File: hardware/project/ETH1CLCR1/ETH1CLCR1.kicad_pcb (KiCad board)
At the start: 6 copper layers, 160 x 100 mm, 705 parts, among them J1201 C64AC, J1301 Conn_02x05, J301 Conn_02x01, J302 Conn_02x05, J601 Conn_02x05, K1201 HE3621A0510, K1202 HE3621A0510, K1203 HE3621A0510, K1204 HE3621A0510, K1205 HE3621A0510, K1206 HE3621A0510, K701 9012, K702 9012, K703 9012, K704 9012, K801 TQ2SA-5V, M101 60817-096, Q1101 BC847, Q1102 BC847, Q1103 BC847, Q1104 BC847, Q501 IRFR5410, Q701 BC847, Q702 BC847, Q703 BC847, Q704 BC847, Q705 MMBT4401L, Q706 MMBT4403L, Q801 BC847W, Q802 2N2218A, Q803 2N2904A, Q804 BC847W, Q805 BC847W, Q806 BC847W, Q807 BC847W, Q808 BC847W, Q901 BC847W, Q902 BC847W, Q903 BC847W, U1001 TL074, U1002 TL074, U1003 REF192, U1004 DAC8568IBPWR, U1101 ADG419BR, U1102 ADG419BR, U1103 REF192, U1104 AD8606-2-MSOP, U1105 AD8606-2-MSOP, U1106 AD7380, U1107 AD8605, U1108 LT6350, U1109 LT6350, U1110 OPA602, U1111 OPA602, U1112 PGA103, U1113 PGA103, U1201 ULN2003A, U1301 24LC08B-E/MS, U1302 STM32H743ZI, U1401 ECS-3225SMV-500-GP-TR, U1402 REF192, U1403 74AHCT1G08, U1404 AD5689BRUZ, U1405 AD9835, U1406 TL072, U1407 DG419LDY, U1408 AD5453YRMZ, U1409 LT1468, U1410 LT1468, U1411 LT1468, U1501 LT8330_S6, U1502 LT8330_S6, U1503 MC7815BD2TG, U1504 MC7915BD2TG, U1505 MC78M12ABDTRKG, U1506 MC79M12CDTG, U1507 TSR2-2450, U1508 TSR1-2490, U1509 LM1117IMP-3.3/NOPB, U1510 LM1117IMP-3.3/NOPB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

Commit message: Checked the schematics. Created BOM.
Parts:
- removed the C1433 at (331.2, 11.4)
- removed the C1434 at (313.6, 17.0)
- added C1410: 100n, Capacitor_SMD:C_0603_1608Metric_Pad1.05x0.95mm_HandSolder, F.Cu at (166.9, 148.3)
- added C1417: 10n, Capacitor_SMD:C_0603_1608Metric_Pad1.05x0.95mm_HandSolder, F.Cu at (171.6, 145.4)
- added C1435: 10u, Capacitor_SMD:C_0805_2012Metric_Pad1.15x1.40mm_HandSolder, F.Cu at (167.1, 145.6)
- added C607: 1u, Capacitor_SMD:C_0603_1608Metric_Pad1.05x0.95mm_HandSolder, F.Cu at (37.2, 119.5)
- added R1422: DNP, Resistor_SMD:R_0603_1608Metric_Pad1.05x0.95mm_HandSolder, F.Cu at (173.1, 149.4)
- C1434: renamed from C1431; value C -> 1p5
- C1436: renamed from C1435; value C -> 1p5
- D705, D706: value 1N4149 -> 1N4148
- D707, D708: value SML4757A -> CMDZ5256B TR; footprint Diode_SMD:D_SMA -> Diode_SMD:D_SOD-323_HandSoldering
- J1301, J302, J601: value Conn_02x05 -> 20021111-00010T4LF
- Q1101, Q1102, Q1103, Q1104, Q701, Q702, Q703, Q704: value BC847 -> BC847W; footprint Package_TO_SOT_SMD:SOT-23 -> Package_TO_SOT_SMD:SOT-323_SC-70
- R1403, R1404, R912, R915, R918: value NC -> DNP
- R1420, R1421: value R -> 0
- R1428: renamed from R1427; value R -> DNP
- R824: value RN732BTTD9002B25 -> 90k
- R825, R830: value RN732ATTE1002B25 -> 10k
- R826: value RP73PF2A10RBTDF -> 10
- R827: value RT1206BRB07100RL -> 100
- R828: value TNPW08051K01BEEA -> 1k01
- R829: value RN73R2BTTD1001B25 -> 1k
- R906, R908, R909, R910, R911, R913, R917, R919: value RQ73C2A3K01BTDF -> 3k01
- R921, R923: value PAT1206E9000BST1 -> 900
- R922, R924: value RN73R2BTTD1000B25 -> 100
- U1509, U1510: value LM1117IMP-3.3/NOPB -> LM1117DTX-3.3/NOPB
- U1511: value LM1117IMP-5.0/NOPB -> LM1117DTX-5.0/NOPB
- U503: value LM1117IMP-3.3/NOPB -> LM1117DTX-3.3/NOPB; footprint Package_TO_SOT_SMD:SOT-223-3_TabPin2 -> Package_TO_SOT_SMD:TO-252-2
- moved Q702 203.2 mm to (256.5, 79.8)
- moved Q701 203.2 mm to (256.5, 76.2)
- moved Q703 203.2 mm to (261.0, 76.2)
- moved Q704 198.8 mm to (261.0, 79.8)
- moved Q1102 85.7 mm to (21.3, 123.7), turned to 0 degrees
- moved Q1103 82.3 mm to (25.7, 120.1), turned to 0 degrees
- moved Q1101 81.3 mm to (21.3, 120.1), turned to 0 degrees
- moved Q1104 76.3 mm to (25.7, 123.7), turned to 0 degrees
- moved U503 1.97 mm to (203.6, 119.8)
- renumbered C1403 to C1402, C1402 to C1403, C1406 to C1405, C1405 to C1406, C1410 to C1412, C1414 to C1413, C1412 to C1414, C1413 to C1416, C1416 to C1418, C1417 to C1419, C1418 to C1420, C1419 to C1421, C1420 to C1422, C1422 to C1423, C1421 to C1424, C1423 to C1425, C1425 to C1426, C1424 to C1427, C1426 to C1428, C1427 to C1429, C1429 to C1430, C1428 to C1431, C1430 to C1432, C1432 to C1433, C607 to C608, C608 to C609, C609 to C610, C610 to C611, C611 to C612, R1409 to R1407, R1407 to R1408, R1408 to R1409, R1413 to R1411, R1411 to R1412, R1412 to R1413, R1422 to R1423, R1423 to R1424, R1424 to R1425, R1425 to R1426, R1426 to R1427
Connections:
- net /FGEN Buffer + Source resistor/SR100CTR renamed /FGEN Buffer + Source resistor/SR_100CTR
- net /FGEN Buffer + Source resistor/SR10CTR renamed /FGEN Buffer + Source resistor/SR_10CTR
- net /FGEN Buffer + Source resistor/SR10KCTR renamed /FGEN Buffer + Source resistor/SR_10KCTR
- net /FGEN Buffer + Source resistor/SR1KCTR renamed /FGEN Buffer + Source resistor/SR_1KCTR
- net /MCU2/HA3-COMP renamed /MCU2/RR_HA3-COMP
- net /MCU2/R100CRT renamed /MCU2/RR_100CRT
- net /MCU2/R100KCRT renamed /MCU2/RR_100KCRT
- net /MCU2/R10CRT renamed /MCU2/RR_10CRT
- net /MCU2/R10KCRT renamed /MCU2/RR_10KCRT
- net /MCU2/R1KCRT renamed /MCU2/RR_1KCRT
- net /MCU2/RELAY_CTR renamed /MCU2/RR_RELAYCTR
- U1405 pad 3: (no net) -> Net-(C1417-Pad1)

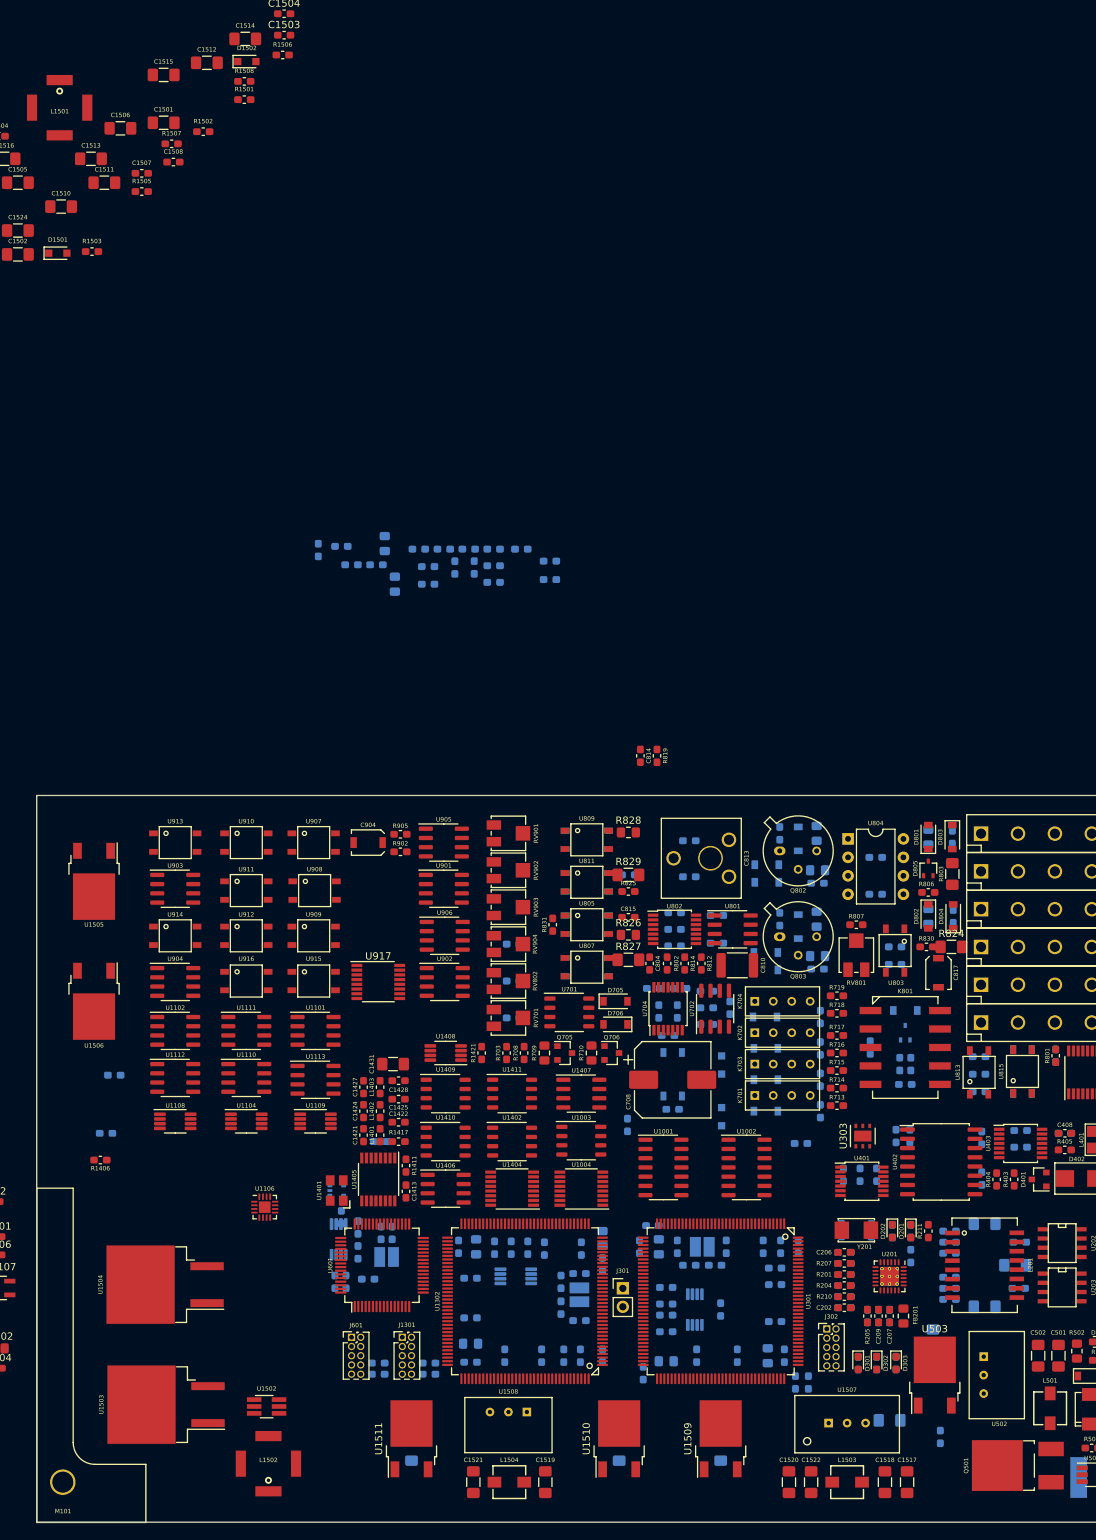
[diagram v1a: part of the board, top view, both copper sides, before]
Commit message: Fixed some mistakes in the foorpeints. BOM list ready.
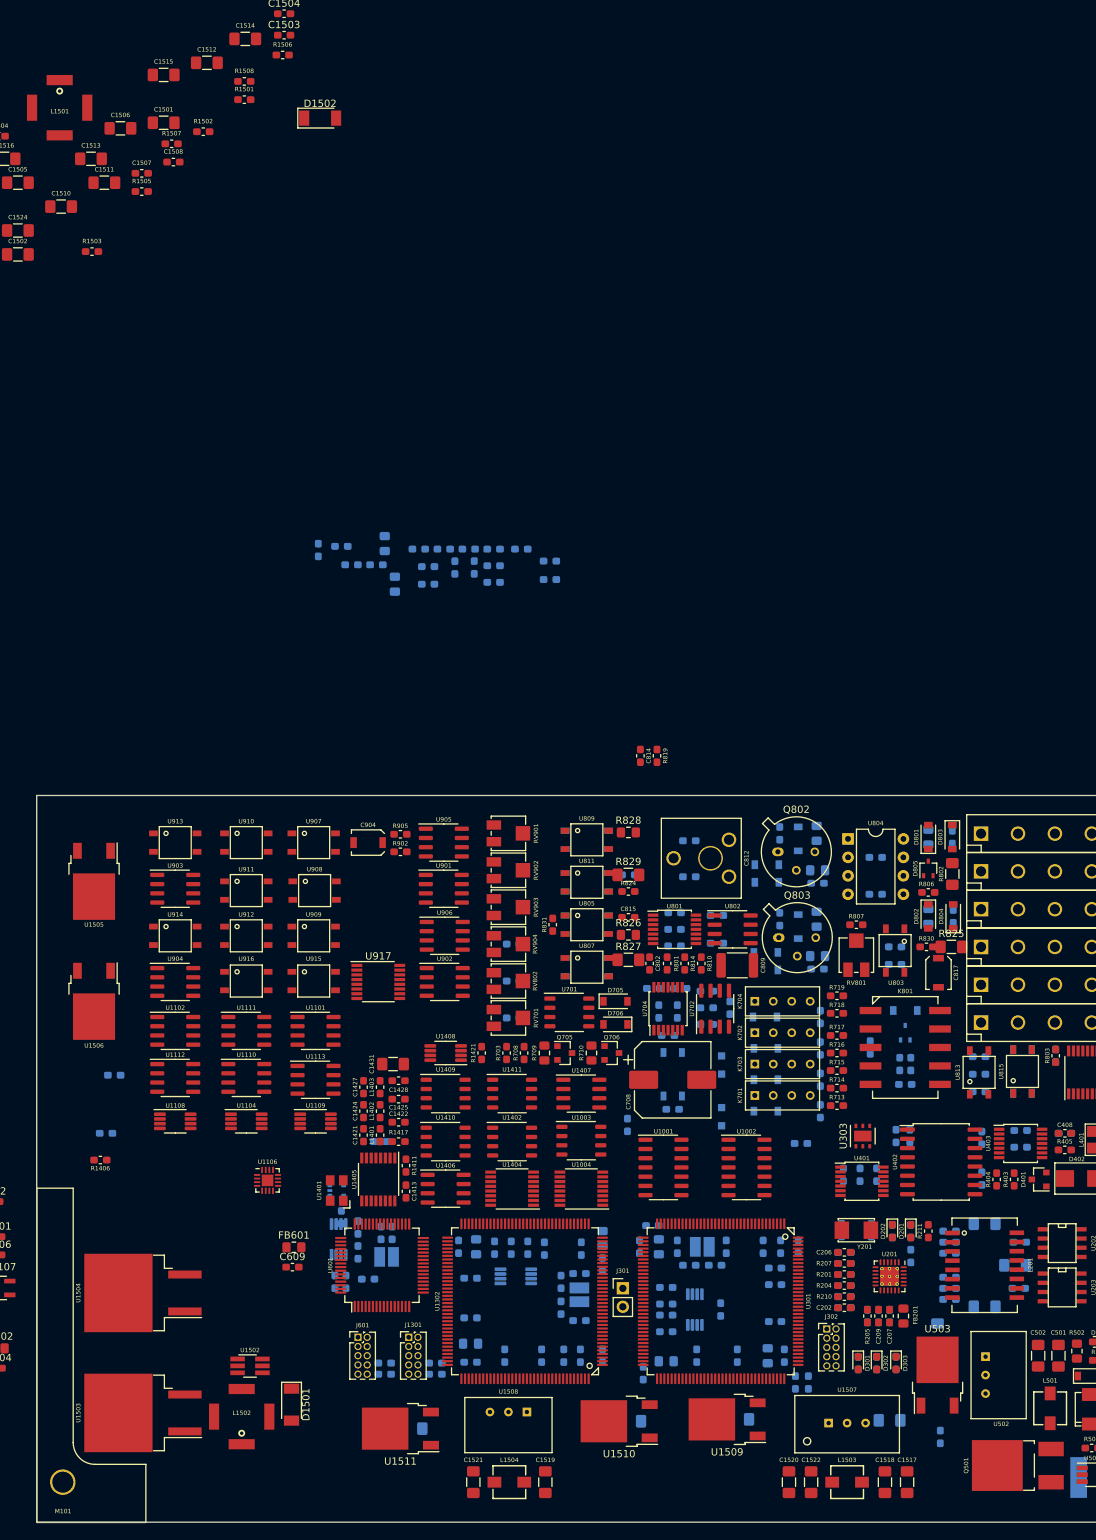
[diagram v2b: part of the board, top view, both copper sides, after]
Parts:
- added C609: 1u, Capacitor_SMD:C_0603_1608Metric_Pad1.05x0.95mm_HandSolder, F.Cu at (115.2, 104.9)
- added FB601: 742792031, Inductor_SMD:L_0805_2012Metric_Pad1.15x1.40mm_HandSolder, F.Cu at (115.4, 102.2)
- C708: value EEHZC1V221V -> 220u
- C713: value 43p/300V -> 43p/200V
- C809: renamed from C810; value 1u/150V -> 1u/100V
- C814: value 33p/300V -> 33p/200V
- D1501, D1502: value PMEG6010CEJ -> PMEG6010EP,115; footprint Diode_SMD:D_SOD-323_HandSoldering -> Diode_SMD:D_SOD-128
- R801: renamed from R802; value 1k -> 2k2
- moved D1501 161.7 mm to (115.1, 123.8), turned to 270 degrees
- moved D1502 12.7 mm to (119.0, -53.2)
- moved L1502 7.45 mm to (108.2, 125.5)
- moved U1502 6.04 mm to (109.3, 118.5)
- moved C1525 4.84 mm to (176.5, 125.9), turned to 0 degrees
- moved C1526 4.22 mm to (161.7, 126.1), turned to 0 degrees
- moved U1106 3.70 mm to (111.8, 93.0)
- moved U1503 3.37 mm to (94.6, 125.0)
- moved U1504 3.26 mm to (94.6, 108.5)
- moved C1527 2.92 mm to (131.6, 127.1), turned to 0 degrees
- moved U1509 2.81 mm to (175.0, 125.9), turned to 180 degrees
- moved U1510 2.41 mm to (160.1, 126.1), turned to 180 degrees
- moved U1511 2.07 mm to (130.0, 127.1), turned to 180 degrees
- moved C504 1.05 mm to (204.0, 114.1)
- moved J1301 0.89 mm to (131.2, 114.6)
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- renumbered C609 to C610, C610 to C611, C611 to C612, C612 to C613, C804 to C802, C805 to C803, C806 to C804, C802 to C805, C803 to C806, C809 to C810, C812 to C811, C813 to C812, C811 to C813, R803 to R802, R801 to R803, R809 to R808, R808 to R809, R812 to R810, R810 to R811, R811 to R812, R825 to R824, R824 to R825, U802 to U801, U801 to U802
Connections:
- net /MCU2/PA_NULL renamed /MCU2/PA_ER
- net /Process Amplifier/NULL_NPN renamed /Process Amplifier/ER_NPN
- Q802 pad 1: Net-(D806-Pad2) -> Net-(D810-Pad2)
- Q802 pad 2: Net-(D810-Pad2) -> Net-(D806-Pad2)
- Q803 pad 1: Net-(D807-Pad1) -> Net-(D811-Pad1)
- Q803 pad 2: Net-(D811-Pad1) -> Net-(D807-Pad1)
- R946 pad 1: /ADC/Eref -> Net-(R946-Pad1)
- U601 pad 13: +3.3VF -> /MCU3/VDDA
- U916 pad 3: AGNDF -> Net-(R946-Pad1)
- U916 pad 4: /ADC/Em -> /ADC/Eref

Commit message: PCB layout
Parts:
- removed M101: 60817-096, ETH1CLCR1:60817-096
- added C1506: 10u/50V, Capacitor_SMD:C_1206_3216Metric_Pad1.42x1.75mm_HandSolder, F.Cu at (97.4, 123.3)
- added C1507: 10u/50V, Capacitor_SMD:C_1206_3216Metric_Pad1.42x1.75mm_HandSolder, F.Cu at (114.8, 133.5)
- added C715: 10u/35V, Capacitor_SMD:C_1206_3216Metric_Pad1.42x1.75mm_HandSolder, F.Cu at (54.2, 36.4)
- added C716: 10u/35V, Capacitor_SMD:C_1206_3216Metric_Pad1.42x1.75mm_HandSolder, F.Cu at (54.2, 39.7)
- added C823: 10u/35V, Capacitor_SMD:C_1206_3216Metric_Pad1.42x1.75mm_HandSolder, B.Cu at (195.5, 45.2)
- added C824: 10u/35V, Capacitor_SMD:C_1206_3216Metric_Pad1.42x1.75mm_HandSolder, B.Cu at (195.5, 50.8)
- C1514: renamed from C1505; moved to B.Cu
- C1515: renamed from C1506; moved to B.Cu
- C1516: renamed from C1507; moved to B.Cu
- C1519: renamed from C1509; moved to B.Cu
- C1520: renamed from C1510; moved to B.Cu
- C1522: renamed from C1511; moved to B.Cu
- C1523: renamed from C1512; moved to B.Cu
- C1524: renamed from C1513; moved to B.Cu
- C1525: renamed from C1514; moved to B.Cu
- C1526: renamed from C1524; moved to B.Cu
- C322, C609, C705, C706, C814, D1501, D1502, FB601, Q701, Q702, Q703, Q704, R1506, R1507, R1508, R819, R825, R902, R905, U908, U910, U912: moved to B.Cu
- C816: moved to F.Cu
- moved Q801 227.6 mm to (219.7, 79.6), turned to 270 degrees
- moved R1506 197.5 mm to (84.2, 133.3), turned to 90 degrees
- moved R1501 189.5 mm to (95.8, 133.3), turned to 270 degrees
- moved R1504 186.5 mm to (104.5, 133.3)
- moved R1502 184.8 mm to (98.2, 133.3), turned to 90 degrees
- moved U1504 184.4 mm to (91.1, 133.3)
- moved C1525 182.6 mm to (112.4, 118.5), turned to 180 degrees
- moved C1510 181.1 mm to (97.4, 128.5), turned to 270 degrees
- moved L1502 180.7 mm to (90.6, 125.9), turned to 270 degrees
- moved C1516 179.1 mm to (86.5, 133.3), turned to 270 degrees
- moved C1515 179.0 mm to (112.1, 126.0), turned to 180 degrees
- moved R1508 177.7 mm to (104.6, 119.4)
- moved R1505 176.6 mm to (86.5, 133.3), turned to 270 degrees
- moved D1502 175.8 mm to (88.5, 119.9), turned to 270 degrees
- moved C1523 175.6 mm to (107.6, 114.7), turned to 270 degrees
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- renumbered C1517 to C1501, C1518 to C1502, C1520 to C1503, C1522 to C1504, C1523 to C1505, C1525 to C1508, C1526 to C1509, C1501 to C1510, C1502 to C1511, C1503 to C1512, C1504 to C1513, C1508 to C1517, C1519 to C1518, C1515 to C1527, C1516 to C1528, C1527 to C1529, L1503 to L1501, L1501 to L1502, L1502 to L1503, U1507 to U1501, U1509 to U1502, U1510 to U1503, U1501 to U1504, U1502 to U1505, U1503 to U1506, U1504 to U1507, U1511 to U1509, U1505 to U1510, U1506 to U1511

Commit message: PCB layout
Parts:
- added C1437: 100n, Capacitor_SMD:C_0603_1608Metric_Pad1.05x0.95mm_HandSolder, B.Cu at (135.3, 75.2)
- added C1438: 100n, Capacitor_SMD:C_0603_1608Metric_Pad1.05x0.95mm_HandSolder, B.Cu at (145.4, 89.8)
- added C911: 100n, Capacitor_SMD:C_0603_1608Metric_Pad1.05x0.95mm_HandSolder, B.Cu at (135.6, 44.3)
- added C912: 100n, Capacitor_SMD:C_0603_1608Metric_Pad1.05x0.95mm_HandSolder, B.Cu at (135.6, 54.6)
- added C913: 100n, Capacitor_SMD:C_0603_1608Metric_Pad1.05x0.95mm_HandSolder, B.Cu at (135.6, 59.6)
- added C914: 100n, Capacitor_SMD:C_0603_1608Metric_Pad1.05x0.95mm_HandSolder, B.Cu at (135.6, 67.1)
- added C915: 100n, Capacitor_SMD:C_0603_1608Metric_Pad1.05x0.95mm_HandSolder, B.Cu at (112.0, 48.8)
- added C916: 100n, Capacitor_SMD:C_0603_1608Metric_Pad1.05x0.95mm_HandSolder, B.Cu at (112.0, 60.6)
- added C917: 100n, Capacitor_SMD:C_0603_1608Metric_Pad1.05x0.95mm_HandSolder, B.Cu at (135.6, 57.1)
- added C918: 100n, Capacitor_SMD:C_0603_1608Metric_Pad1.05x0.95mm_HandSolder, B.Cu at (135.6, 64.0)
- added C919: 100n, Capacitor_SMD:C_0603_1608Metric_Pad1.05x0.95mm_HandSolder, B.Cu at (135.6, 69.6)
- added C920: 100n, Capacitor_SMD:C_0603_1608Metric_Pad1.05x0.95mm_HandSolder, B.Cu at (112.0, 44.2)
- added C921: 100n, Capacitor_SMD:C_0603_1608Metric_Pad1.05x0.95mm_HandSolder, B.Cu at (135.6, 48.1)
- added C922: 100n, Capacitor_SMD:C_0603_1608Metric_Pad1.05x0.95mm_HandSolder, B.Cu at (112.0, 56.8)
- added C923: 100n, Capacitor_SMD:C_0603_1608Metric_Pad1.05x0.95mm_HandSolder, B.Cu at (124.0, 66.5)
- added R1141: 10k, Resistor_SMD:R_0603_1608Metric_Pad1.05x0.95mm_HandSolder, F.Cu at (118.9, 70.2)
- added R1142: 10K, Resistor_SMD:R_0603_1608Metric_Pad1.05x0.95mm_HandSolder, F.Cu at (106.4, 70.2)
- C1001, C1006, C1008, C1019, C1020, C1021, C1111, C1114, C1115, C1118, C1121, C1122, C1123, C1125, C1126, C1129, C1130, C1410, C1434, C1435, C1512, C1513, C1527, C1528, C607, C715, C716, C819, C820, C821, C822, C908, C909, C910, Q902, Q903, R1018, R1019, R1024, R1025, R1113, R1114, R1119, R1120, R1122, R1124, R1129, R1130, R1131, R1133, R1135, R1136, R1139, R1140, R1406, R1422, R913, R918, R949, R950: moved to B.Cu
- C1108: value 1u -> 100n; moved to B.Cu
- C1109, C1110, C1113: value 1u -> 100n
- C1414, C1416, C901, C905, C906, D1401, R1001, R1003, R1407, R1409, R1412, R1413, R1423, R1424, R1425, R1426, R1427, R903, R904, R906, R907, R908, R917, R921, R922, R923, R927, R929, R931, R935, R937, R938, R944: moved to F.Cu
- R1428: value DNP -> 10k
- moved C1416 203.7 mm to (130.7, 95.8)
- moved C1513 200.0 mm to (103.8, 132.2)
- moved C1512 200.0 mm to (95.4, 134.5), turned to 270 degrees
- moved C1412 198.5 mm to (130.7, 89.2), turned to 270 degrees
- moved D1401 198.1 mm to (135.3, 98.6), turned to 0 degrees
- moved R1415 191.0 mm to (139.2, 95.5)
- moved C1433 189.5 mm to (154.1, 81.0)
- moved R1428 188.0 mm to (150.6, 79.1)
- moved R1414 187.3 mm to (140.7, 95.5)
- moved R922 182.4 mm to (144.1, 46.2), turned to 90 degrees
- moved R914 181.2 mm to (142.7, 52.3), turned to 270 degrees
- moved R1018 177.2 mm to (179.1, 88.8), turned to 90 degrees
- moved R921 176.0 mm to (141.2, 46.2), turned to 270 degrees
- moved C1007 174.1 mm to (154.1, 93.9)
- moved R925 174.1 mm to (119.1, 45.7), turned to 270 degrees
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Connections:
- U1101 pad 2: AGNDF -> Net-(R1142-Pad2)
- U1102 pad 2: AGNDF -> Net-(R1141-Pad2)
- U1106 pad 5: Net-(R1108-Pad2) -> Net-(R1106-Pad2)
- U1106 pad 6: Net-(R1107-Pad2) -> Net-(R1105-Pad2)
- U1106 pad 7: Net-(R1106-Pad2) -> Net-(R1108-Pad2)
- U1106 pad 8: Net-(R1105-Pad2) -> Net-(R1107-Pad2)

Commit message: PCB layout
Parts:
- C1103, C1104, C1105, C1106, C1107, C1110, C1112, C1113, C1116, C1117, C1119, C1120, D1401, U1107: moved to B.Cu
- C606, R940, U1403: moved to F.Cu
- moved C1117 81.2 mm to (86.2, 97.4), turned to 270 degrees
- moved R1112 80.7 mm to (95.8, 90.6)
- moved C1119 79.3 mm to (97.9, 87.1), turned to 270 degrees
- moved R1111 77.0 mm to (95.8, 92.3)
- moved R1107 75.4 mm to (99.4, 92.3)
- moved C1110 72.7 mm to (106.6, 89.4), turned to 90 degrees
- moved C1112 71.3 mm to (96.6, 91.4), turned to 90 degrees
- moved R1104 69.8 mm to (95.8, 95.9), turned to 180 degrees
- moved R1108 68.7 mm to (99.4, 90.6)
- moved C1120 67.7 mm to (97.5, 99.6)
- moved C1113 66.3 mm to (105.7, 94.1), turned to 270 degrees
- moved C1107 66.1 mm to (102.6, 94.1), turned to 270 degrees
- moved C1103 65.3 mm to (104.3, 89.4), turned to 90 degrees
- moved C1105 64.4 mm to (101.9, 89.4), turned to 90 degrees
- moved R1103 64.2 mm to (99.3, 95.9)
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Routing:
- net +3V3: track 0.00 -> 87.3 mm, vias 0 -> 36
- net +24VDD: track 0.00 -> 72.8 mm, vias 0 -> 32
- net AGNDF: track 0.00 -> 27.7 mm, vias 0 -> 19
- net +3.3VP: track 0.00 -> 23.4 mm, vias 0 -> 15
- net +5VF: track 0.00 -> 23.4 mm, vias 0 -> 15
- net +3.3VF: track 0.00 -> 23.4 mm, vias 0 -> 15
- net VCCQ: track 0.00 -> 19.1 mm, vias 0 -> 5
- net Net-(C502-Pad1): track 0.00 -> 19.1 mm, vias 0 -> 11
- net +5V_TRIG: track 0.00 -> 11.8 mm, vias 0 -> 4
- net Net-(C204-Pad1): track 0.00 -> 10.6 mm, vias 0 -> 1
- net Net-(C201-Pad1): track 0.00 -> 10.5 mm, vias 0 -> 1
- net /MCU1/MCU_VDDA: track 0.00 -> 8.91 mm, vias 0 -> 1
- net Net-(C1505-Pad1): track 0.00 -> 7.25 mm, vias 0 -> 5
- net Net-(D201-Pad2): track 0.00 -> 6.40 mm
- net Net-(C305-Pad1): track 0.00 -> 6.04 mm, vias 0 -> 1
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- added copper zone on B.Cu, net +24VDD
- added copper zone on F.Cu, net +24VDD
- added copper zone on Mixed, net +24VDD
- added copper zone on Power_A, net +24VDD
- added copper zone on Power_B, net +24VDD
- added copper zone on B.Cu, net +3.3VF
- added copper zone on F.Cu, net +3.3VF
- added copper zone on Power_A, net +3.3VF
- added copper zone on B.Cu, net +3.3VP
- added copper zone on F.Cu, net +3.3VP
- added copper zone on Power_B, net +3.3VP
- added copper zone on B.Cu, net +3V3
- added copper zone on F.Cu, net +3V3
- added copper zone on Power_A, net +3V3
- added copper zone on B.Cu, net +5V
- added copper zone on F.Cu, net +5V
- added copper zone on Power_A, net +5V
- added copper zone on B.Cu, net +5VF
- added copper zone on F.Cu, net +5VF
- added copper zone on Power_A, net +5VF
- added copper zone on Power_A, net +5V_TRIG
- added copper zone on B.Cu, net AGNDF
- added copper zone on F.Cu, net AGNDF
- added copper zone on GNB_B, net AGNDF
- added copper zone on GND_A, net AGNDF
- added copper zone on GND_A, net GND_TRIG
- added copper zone on F.Cu, net Net-(C1503-Pad1)
- added copper zone on B.Cu, net Net-(C1505-Pad1)
- added copper zone on F.Cu, net Net-(C1505-Pad1)
- added copper zone on Mixed, net Net-(C1505-Pad1)
- added copper zone on F.Cu, net Net-(C1521-Pad1)
- added copper zone on B.Cu, net Net-(C502-Pad1)
- added copper zone on F.Cu, net Net-(C502-Pad1)
- added copper zone on Power_B, net Net-(C502-Pad1)
- added copper zone on F.Cu, net Net-(D501-Pad1)
- added copper zone on Power_B, net VCCQ
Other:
- copper layers 6 -> 8
- net class Connector added: clearance 0.508, trace_width 0.127, via_dia 0.5, via_drill 0.2
